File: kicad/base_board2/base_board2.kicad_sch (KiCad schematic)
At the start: 26 parts, among them J1 Conn_02x04_Odd_Even, J2 Conn_01x02, SW1 SW_Push, SW2 SW_Push, SW3 SW_Push, SW4 SW_Push, U1 IS31FL3743A, U2 LED matrix 15x10

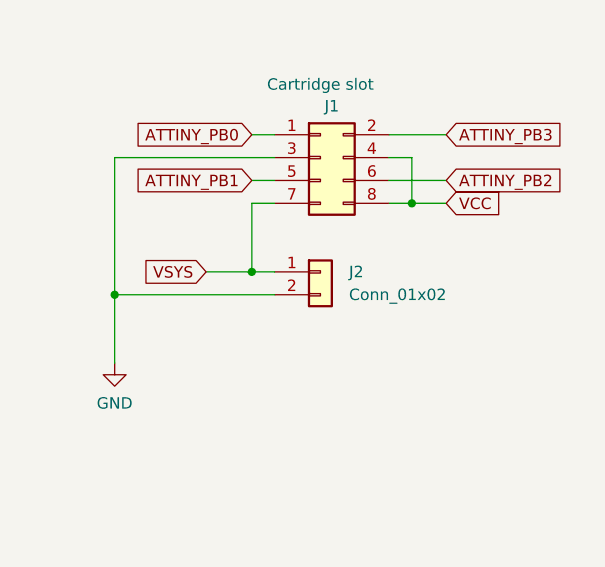
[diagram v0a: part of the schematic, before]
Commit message: playable brik.S; resistor ladder change for wider voltage gap between keys
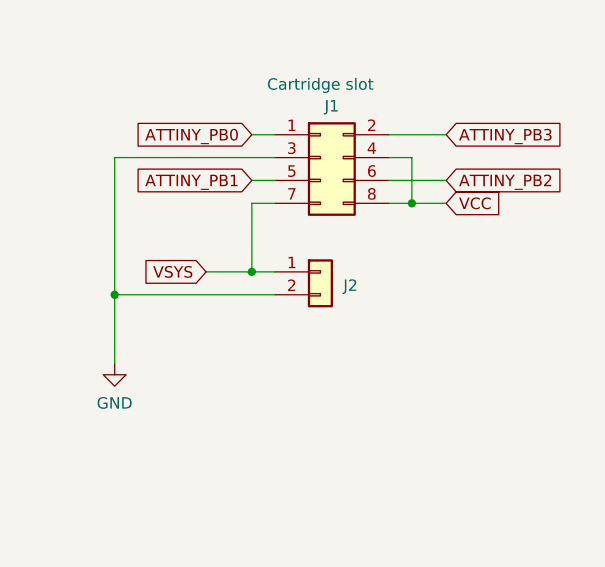
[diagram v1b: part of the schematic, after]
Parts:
- J2: footprint Connector_PinHeader_2.54mm:PinHeader_1x02_P2.54mm_Vertical -> components:Pads_2_54_2x
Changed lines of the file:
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@@
 		(on_board yes)
 		(dnp no)
-		(fields_autoplaced yes)
 		(property "Reference" "J2"
-			(at 231.775 105.41 0)
+			(at 231.14 106.934 0)
 			(effects
 				(font
@@
 				)
 				(justify left)
+				(hide yes)
 			)
 		)
-		(property "Footprint" "Connector_PinHeader_2.54mm:PinHeader_1x02_P2.54mm_Vertical"
+		(property "Footprint" "components:Pads_2_54_2x"
 			(at 228.6 105.41 0)
 			(effects

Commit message: fix an oopsie on base_board2
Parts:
- removed R6: 2K2, Resistor_SMD:R_0603_1608Metric, symbol Device:R
- J2: footprint components:Pads_2_54_2x -> components:Pads_1x2mm_2x
- R4: value 8K2 -> 15K
- R6: renamed from R7; value 2K2 -> 4K7
- R7: renamed from R8; value 2K2 -> 10K
- R8: renamed from R9; value 8K2 -> 47K
- R9: renamed from R10; value 4K7 -> 680K
- renumbered R11 to R10
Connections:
- net SDB is gone; now on net VCC: U1.26 (SDB)
- net ATTINY_PB0: now also R6.1, SW1.2
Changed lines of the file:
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@@
 	(wire
 		(pts
+			(xy 118.11 63.5) (xy 118.11 73.66)
+		)
+		(stroke
+			(width 0)
+			(type default)
+		)
+	)
+	(wire
+		(pts
 			(xy 149.86 121.92) (xy 149.86 111.125)
 		)
@@
 	(wire
 		(pts
-			(xy 100.33 63.5) (xy 105.41 63.5)
-		)
-		(stroke
-			(width 0)
-			(type default)
-		)
-	)
-	(wire
-		(pts
-			(xy 149.86 132.08) (xy 149.86 133.985)
+			(xy 100.33 63.5) (xy 118.11 63.5)
 		)
 		(stroke
@@
 	(wire
 		(pts
-			(xy 149.86 121.92) (xy 149.86 124.46)
+			(xy 72.39 141.605) (xy 72.39 133.985)
 		)
 		(stroke
@@
 	(wire
 		(pts
-			(xy 72.39 141.605) (xy 72.39 133.985)
+			(xy 31.75 49.53) (xy 31.75 52.07)
 		)
 		(stroke
@@
 	(wire
 		(pts
-			(xy 31.75 49.53) (xy 31.75 52.07)
+			(xy 242.57 30.48) (xy 247.65 30.48)
 		)
 		(stroke
@@
 	(wire
 		(pts
-			(xy 242.57 30.48) (xy 247.65 30.48)
+			(xy 149.86 121.92) (xy 149.86 133.985)
 		)
 		(stroke
@@
 		)
 	)
-	(global_label "SDB"
-		(shape input)
-		(at 105.41 63.5 0)
-		(fields_autoplaced yes)
-		(effects
-			(font
-				(size 1.27 1.27)
-			)
-			(justify left)
-		)
-		(property "Intersheetrefs" "${INTERSHEET_REFS}"
-			(at 112.1447 63.5 0)
-			(effects
-				(font
-					(size 1.27 1.27)
-				)
-				(justify left)
-				(hide yes)
-			)
-		)
-	)
 	(global_label "C6"
 		(shape input)
@@
 		(dnp no)
 		(fields_autoplaced yes)
-		(property "Reference" "#PWR0101"
+		(property "Reference" "#PWR01"
 			(at 31.75 83.82 0)
 			(effects
@@
 			(project "base_board2"
 				(path "/18190135-c25a-4997-9fef-a70445b975f2"
-					(reference "#PWR0101")
+					(reference "#PWR01")
 					(unit 1)
 				)
@@
 		(dnp no)
 		(fields_autoplaced yes)
-		(property "Reference" "R9"
+		(property "Reference" "R8"
 			(at 152.4 165.1 0)
 			(effects
@@
 			)
 		)
-		(property "Value" "8K2"
+		(property "Value" "47K"
 			(at 152.4 167.64 0)
 			(effects
@@
 			(project "base_board2"
 				(path "/18190135-c25a-4997-9fef-a70445b975f2"
-					(reference "R9")
+					(reference "R8")
 					(unit 1)
 				)
@@
 			)
 		)
-		(property "Footprint" "components:Pads_2_54_2x"
+		(property "Footprint" "components:Pads_1x2mm_2x"
 			(at 228.6 105.41 0)
 			(effects
@@
 		(dnp no)
 		(fields_autoplaced yes)
-		(property "Reference" "R10"
+		(property "Reference" "R9"
 			(at 156.845 116.205 90)
 			(effects
@@
 			)
 		)
-		(property "Value" "4K7"
+		(property "Value" "680K"
 			(at 156.845 118.745 90)
 			(effects
@@
 			(project "base_board2"
 				(path "/18190135-c25a-4997-9fef-a70445b975f2"
-					(reference "R10")
+					(reference "R9")
 					(unit 1)
 				)
@@
 		(dnp no)
 		(fields_autoplaced yes)
-		(property "Reference" "#PWR0105"
+		(property "Reference" "#PWR06"
 			(at 205.74 121.92 0)
 			(effects
@@
 			(project "base_board2"
 				(path "/18190135-c25a-4997-9fef-a70445b975f2"
-					(reference "#PWR0105")
-					(unit 1)
-				)
-			)
-		)
-	)
-	(symbol
-		(lib_id "Device:R")
-		(at 149.86 128.27 0)
-		(unit 1)
-		(exclude_from_sim no)
-		(in_bom yes)
-		(on_board yes)
-		(dnp no)
-		(fields_autoplaced yes)
-		(property "Reference" "R6"
-			(at 152.4 127 0)
-			(effects
-				(font
-					(size 1.27 1.27)
-				)
-				(justify left)
-			)
-		)
-		(property "Value" "2K2"
-			(at 152.4 129.54 0)
-			(effects
-				(font
-					(size 1.27 1.27)
-				)
-				(justify left)
-			)
-		)
-		(property "Footprint" "Resistor_SMD:R_0603_1608Metric"
-			(at 148.082 128.27 90)
-			(effects
-				(font
-					(size 1.27 1.27)
-				)
-				(hide yes)
-			)
-		)
-		(property "Datasheet" "~"
-			(at 149.86 128.27 0)
-			(effects
-				(font
-					(size 1.27 1.27)
-				)
-				(hide yes)
-			)
-		)
-		(property "Description" ""
-			(at 149.86 128.27 0)
-			(effects
-				(font
-					(size 1.27 1.27)
-				)
-			)
-		)
-		(pin "1"
-		)
-		(pin "2"
-		)
-		(instances
-			(project "base_board2"
-				(path "/18190135-c25a-4997-9fef-a70445b975f2"
-					(reference "R6")
+					(reference "#PWR06")
 					(unit 1)
 				)
@@
 		(dnp no)
 		(fields_autoplaced yes)
-		(property "Reference" "R8"
-			(at 152.4 151.13 0)
+		(property "Reference" "R7"
+			(at 152.4 151.1299 0)
 			(effects
 				(font
@@
 			)
 		)
-		(property "Value" "2K2"
-			(at 152.4 153.67 0)
+		(property "Value" "10K"
+			(at 152.4 153.6699 0)
 			(effects
 				(font
@@
 			(project "base_board2"
 				(path "/18190135-c25a-4997-9fef-a70445b975f2"
-					(reference "R8")
+					(reference "R7")
 					(unit 1)
 				)
@@
 		(dnp no)
 		(fields_autoplaced yes)
-		(property "Reference" "R7"
+		(property "Reference" "R6"
 			(at 152.4 138.43 0)
 			(effects
@@
 			)
 		)
-		(property "Value" "2K2"
+		(property "Value" "4K7"
 			(at 152.4 140.97 0)
 			(effects
@@
 			(project "base_board2"
 				(path "/18190135-c25a-4997-9fef-a70445b975f2"
-					(reference "R7")
+					(reference "R6")
 					(unit 1)
 				)
@@
 		(dnp no)
 		(fields_autoplaced yes)
-		(property "Reference" "#PWR0106"
+		(property "Reference" "#PWR04"
 			(at 143.51 96.52 0)
 			(effects
@@
 			(project "base_board2"
 				(path "/18190135-c25a-4997-9fef-a70445b975f2"
-					(reference "#PWR0106")
+					(reference "#PWR04")
 					(unit 1)
 				)
@@
 		(dnp no)
 		(fields_autoplaced yes)
-		(property "Reference" "#PWR0102"
+		(property "Reference" "#PWR02"
 			(at 62.23 168.91 0)
 			(effects
@@
 			(project "base_board2"
 				(path "/18190135-c25a-4997-9fef-a70445b975f2"
-					(reference "#PWR0102")
+					(reference "#PWR02")
 					(unit 1)
 				)
@@
 			)
 		)
-		(property "Value" "8K2"
+		(property "Value" "15K"
 			(at 142.875 118.745 90)
 			(effects
@@
 		(dnp no)
 		(fields_autoplaced yes)
-		(property "Reference" "#PWR0104"
+		(property "Reference" "#PWR05"
 			(at 165.735 137.795 0)
 			(effects
@@
 			(project "base_board2"
 				(path "/18190135-c25a-4997-9fef-a70445b975f2"
-					(reference "#PWR0104")
+					(reference "#PWR05")
 					(unit 1)
 				)
@@
 		(dnp no)
 		(fields_autoplaced yes)
-		(property "Reference" "R11"
+		(property "Reference" "R10"
 			(at 161.29 67.31 0)
 			(effects
@@
 			(project "base_board2"
 				(path "/18190135-c25a-4997-9fef-a70445b975f2"
-					(reference "R11")
+					(reference "R10")
 					(unit 1)
 				)
@@
 		(dnp no)
 		(fields_autoplaced yes)
-		(property "Reference" "#PWR0103"
+		(property "Reference" "#PWR03"
 			(at 133.985 184.785 0)
 			(effects
@@
 			(project "base_board2"
 				(path "/18190135-c25a-4997-9fef-a70445b975f2"
-					(reference "#PWR0103")
+					(reference "#PWR03")
 					(unit 1)
 				)

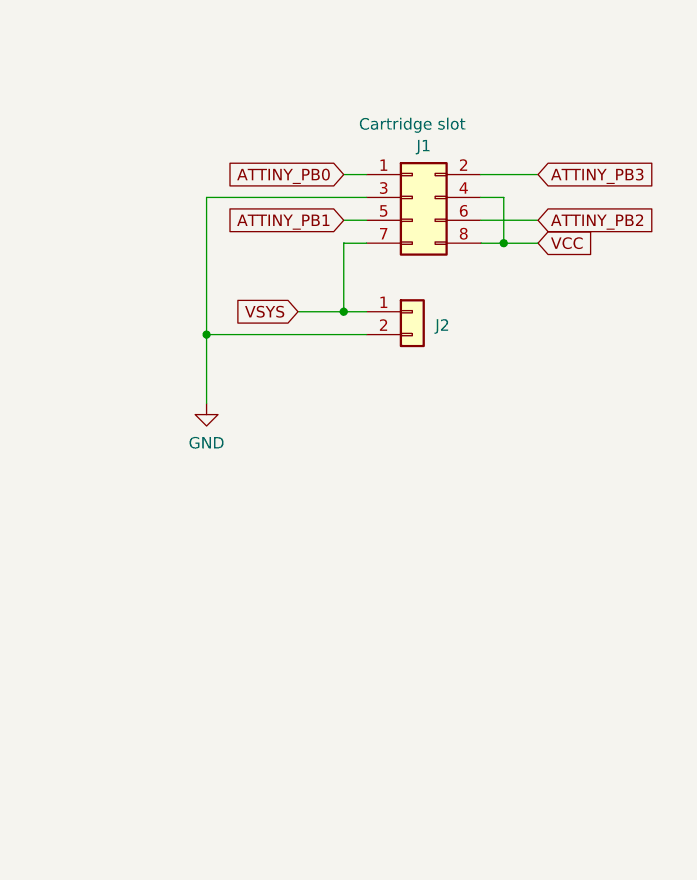
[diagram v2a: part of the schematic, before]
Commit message: pcbs: improve powering scheme, redesign cartridge; 3dcad: update whole housing
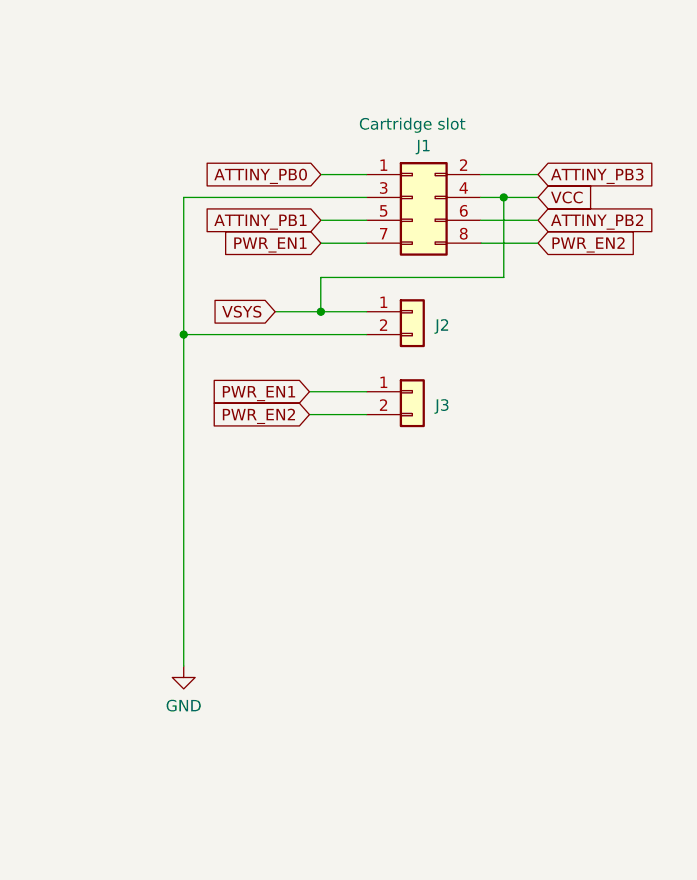
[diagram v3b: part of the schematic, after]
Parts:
- added J3: Conn_01x02, components:Pads_1x2mm_2x, symbol Connector_Generic:Conn_01x02
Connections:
- net VCC: now also J2.1 (Pin_1); no longer J1.8 (Pin_8)
- net VSYS renamed PWR_EN1
- net PWR_EN1: now also J3.1 (Pin_1); no longer J2.1 (Pin_1)
- new net PWR_EN2: J1.8 (Pin_8), J3.2 (Pin_2)
